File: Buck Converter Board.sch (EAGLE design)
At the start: 6 parts, among them J1 POWERPOLE_POWER25A_HORIZONTAL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, J2 POWERPOLE_POWER25A_HORIZONTAL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

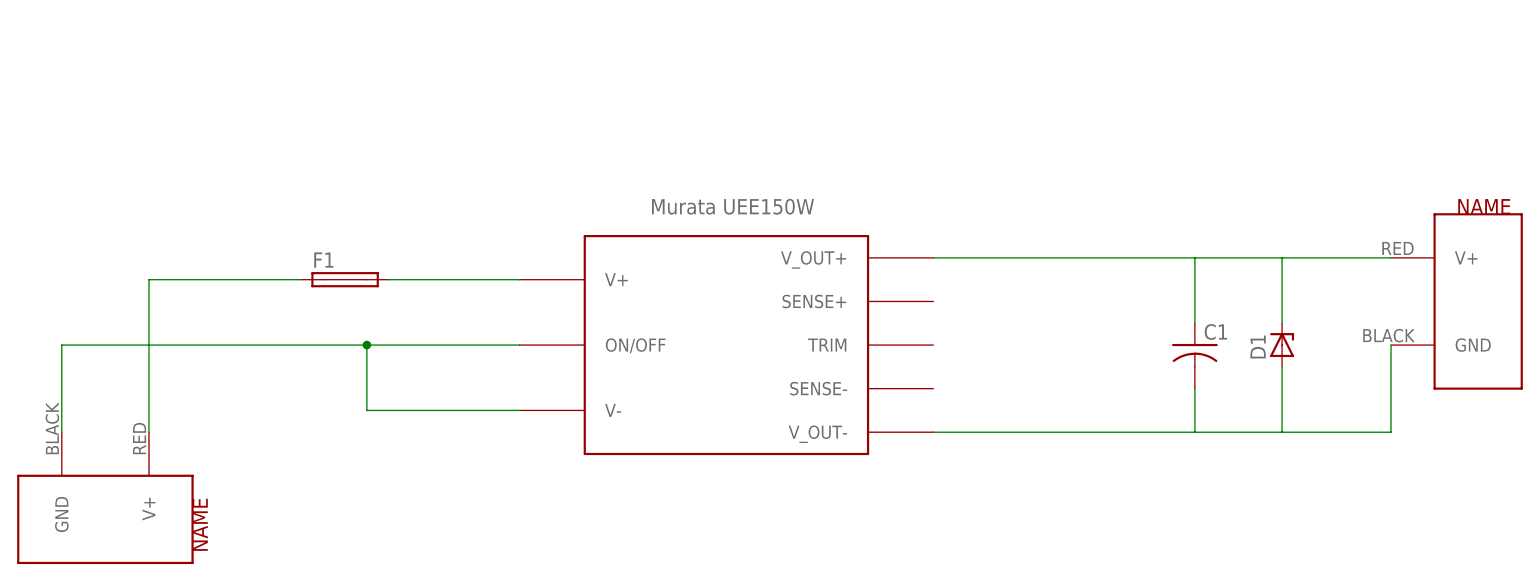
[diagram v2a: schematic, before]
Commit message: routed buck board
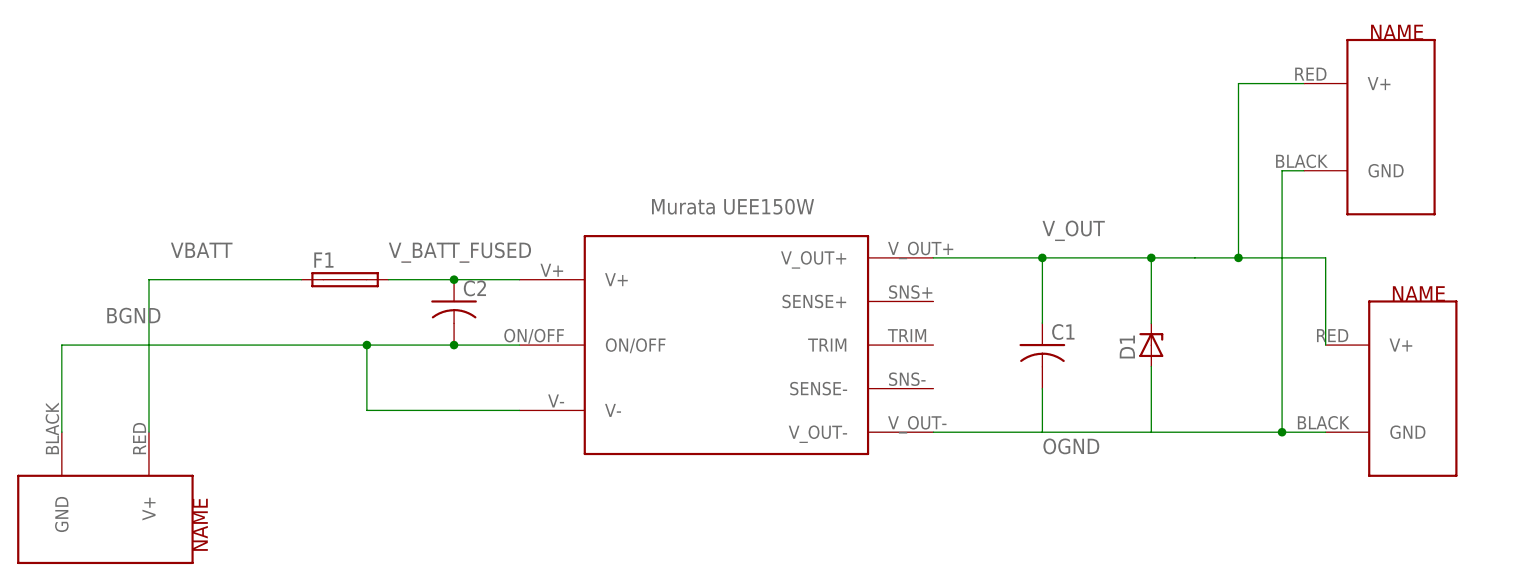
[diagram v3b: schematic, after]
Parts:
- added C2: (no value), rcl:C-USC0805
- added J3: POWERPOLE_POWER25A_HORIZONTAL_G2, powerpoles:POWERPOLE_POWER25A_HORIZONTAL_G2
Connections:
- net N$1 renamed VBATT
- removed net N$11: D1.C
- removed net N$2: F1.2, U$1.V+
- removed net N$3: J1.GND, U$1.ON/OFF, U$1.V-
- removed net N$4: J2.V+, U$1.V_OUT+
- removed net N$5: C1.1
- removed net N$6: C1.2, J2.GND, U$1.V_OUT-
- new net BGND: C2.2, J1.GND, U$1.ON/OFF, U$1.V-
- new net OGND: C1.2, J2.GND, J3.GND, U$1.V_OUT-
- new net V_BATT_FUSED: C2.1, F1.2, U$1.V+
- new net V_OUT: C1.1, D1.C, J2.V+, J3.V+, U$1.V_OUT+
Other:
- moved on the sheet: C1, D1
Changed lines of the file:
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@@
 <part name="J1" library="powerpoles" deviceset="POWERPOLE_POWER" device="25A_HORIZONTAL_G2"/>
 <part name="J2" library="powerpoles" deviceset="POWERPOLE_POWER" device="25A_HORIZONTAL_G2"/>
+<part name="D1" library="diode" library_urn="urn:adsk.eagle:library:210" deviceset="ZENER-DIODE" device="SMB" package3d_urn="urn:adsk.eagle:package:43404/2"/>
+<part name="C2" library="rcl" library_urn="urn:adsk.eagle:library:334" deviceset="C-US" device="C0805" package3d_urn="urn:adsk.eagle:package:23617/2"/>
+<part name="J3" library="powerpoles" deviceset="POWERPOLE_POWER" device="25A_HORIZONTAL_G2"/>
 <part name="U$1" library="REV Aux Circuit" deviceset="UEE150W" device=""/>
-<part name="D1" library="diode" library_urn="urn:adsk.eagle:library:210" deviceset="ZENER-DIODE" device="SMB" package3d_urn="urn:adsk.eagle:package:43404/2"/>
 </parts>
 <sheets>
@@
 <attribute name="NAME" x="29.21" y="64.897" size="1.778" layer="95"/>
 </instance>
-<instance part="C1" gate="G$1" x="132.08" y="55.88"/>
+<instance part="C1" gate="G$1" x="114.3" y="55.88"/>
 <instance part="J1" gate="G$1" x="5.08" y="35.56" rot="R270"/>
-<instance part="J2" gate="G$1" x="165.1" y="60.96"/>
+<instance part="J2" gate="G$1" x="157.48" y="50.8"/>
+<instance part="D1" gate="G$1" x="127" y="55.88" rot="R90"/>
+<instance part="C2" gate="G$1" x="45.72" y="60.96"/>
+<instance part="J3" gate="G$1" x="154.94" y="81.28"/>
 <instance part="U$1" gate="G$1" x="60.96" y="43.18"/>
-<instance part="D1" gate="G$1" x="142.24" y="55.88" rot="R90"/>
 </instances>
 <busses>
 </busses>
 <nets>
-<net name="N$1" class="0">
+<net name="VBATT" class="0">
 <segment>
 <pinref part="J1" gate="G$1" pin="V+"/>
@@
 <wire x1="10.16" y1="45.72" x2="10.16" y2="63.5" width="0.1524" layer="91"/>
 <wire x1="10.16" y1="63.5" x2="27.94" y2="63.5" width="0.1524" layer="91"/>
+<label x="12.7" y="66.04" size="1.778" layer="95"/>
 </segment>
 </net>
-<net name="N$2" class="0">
+<net name="V_BATT_FUSED" class="0">
 <segment>
 <pinref part="F1" gate="G$1" pin="2"/>
-<wire x1="38.1" y1="63.5" x2="53.34" y2="63.5" width="0.1524" layer="91"/>
+<wire x1="38.1" y1="63.5" x2="45.72" y2="63.5" width="0.1524" layer="91"/>
+<pinref part="C2" gate="G$1" pin="1"/>
+<wire x1="45.72" y1="63.5" x2="53.34" y2="63.5" width="0.1524" layer="91"/>
+<junction x="45.72" y="63.5"/>
 <pinref part="U$1" gate="G$1" pin="V+"/>
+<label x="38.1" y="66.04" size="1.778" layer="95"/>
 </segment>
 </net>
-<net name="N$3" class="0">
+<net name="BGND" class="0">
 <segment>
 <pinref part="J1" gate="G$1" pin="GND"/>
@@
 <wire x1="0" y1="55.88" x2="35.56" y2="55.88" width="0.1524" layer="91"/>
 <wire x1="35.56" y1="55.88" x2="35.56" y2="48.26" width="0.1524" layer="91"/>
-<pinref part="U$1" gate="G$1" pin="V-"/>
 <wire x1="35.56" y1="48.26" x2="53.34" y2="48.26" width="0.1524" layer="91"/>
 <junction x="35.56" y="55.88"/>
+<wire x1="35.56" y1="55.88" x2="45.72" y2="55.88" width="0.1524" layer="91"/>
+<pinref part="C2" gate="G$1" pin="2"/>
+<wire x1="45.72" y1="55.88" x2="53.34" y2="55.88" width="0.1524" layer="91"/>
+<junction x="45.72" y="55.88"/>
+<pinref part="U$1" gate="G$1" pin="V-"/>
 <pinref part="U$1" gate="G$1" pin="ON/OFF"/>
-<wire x1="35.56" y1="55.88" x2="53.34" y2="55.88" width="0.1524" layer="91"/>
+<label x="5.08" y="58.42" size="1.778" layer="95"/>
 </segment>
 </net>
-<net name="N$6" class="0">
+<net name="V_OUT" class="0">
 <segment>
-<pinref part="C1" gate="G$1" pin="2"/>
-<wire x1="132.08" y1="50.8" x2="132.08" y2="45.72" width="0.1524" layer="91"/>
-<pinref part="J2" gate="G$1" pin="GND"/>
-<wire x1="154.94" y1="55.88" x2="154.94" y2="45.72" width="0.1524" layer="91"/>
-<wire x1="154.94" y1="45.72" x2="132.08" y2="45.72" width="0.1524" layer="91"/>
-<pinref part="U$1" gate="G$1" pin="V_OUT-"/>
-<wire x1="101.6" y1="45.72" x2="132.08" y2="45.72" width="0.1524" layer="91"/>
-</segment>
-</net>
-<net name="N$4" class="0">
-<segment>
+<wire x1="147.32" y1="55.88" x2="147.32" y2="66.04" width="0.1524" layer="91"/>
+<wire x1="147.32" y1="66.04" x2="137.16" y2="66.04" width="0.1524" layer="91"/>
+<wire x1="137.16" y1="66.04" x2="132.08" y2="66.04" width="0.1524" layer="91"/>
+<wire x1="132.08" y1="66.04" x2="127" y2="66.04" width="0.1524" layer="91"/>
+<pinref part="J2" gate="G$1" pin="V+"/>
+<pinref part="J3" gate="G$1" pin="V+"/>
+<wire x1="127" y1="66.04" x2="114.3" y2="66.04" width="0.1524" layer="91"/>
+<wire x1="114.3" y1="66.04" x2="101.6" y2="66.04" width="0.1524" layer="91"/>
+<wire x1="137.16" y1="66.04" x2="137.16" y2="86.36" width="0.1524" layer="91"/>
+<wire x1="137.16" y1="86.36" x2="144.78" y2="86.36" width="0.1524" layer="91"/>
+<junction x="137.16" y="66.04"/>
 <pinref part="U$1" gate="G$1" pin="V_OUT+"/>
-<wire x1="154.94" y1="66.04" x2="101.6" y2="66.04" width="0.1524" layer="91"/>
-<pinref part="J2" gate="G$1" pin="V+"/>
-</segment>
-</net>
-<net name="N$5" class="0">
-<segment>
+<label x="114.3" y="68.58" size="1.778" layer="95"/>
 <pinref part="C1" gate="G$1" pin="1"/>
-<wire x1="132.08" y1="58.42" x2="132.08" y2="66.04" width="0.1524" layer="91"/>
-</segment>
-</net>
-<net name="N$11" class="0">
-<segment>
+<wire x1="114.3" y1="58.42" x2="114.3" y2="66.04" width="0.1524" layer="91"/>
+<junction x="114.3" y="66.04"/>
 <pinref part="D1" gate="G$1" pin="C"/>
-<wire x1="142.24" y1="58.42" x2="142.24" y2="66.04" width="0.1524" layer="91"/>
+<wire x1="127" y1="58.42" x2="127" y2="66.04" width="0.1524" layer="91"/>
+<junction x="127" y="66.04"/>
 </segment>
 </net>
@@
 <segment>
 <pinref part="D1" gate="G$1" pin="A"/>
-<wire x1="142.24" y1="45.72" x2="142.24" y2="53.34" width="0.1524" layer="91"/>
+<wire x1="127" y1="45.72" x2="127" y2="53.34" width="0.1524" layer="91"/>
 </segment>
 </net>
+<net name="OGND" class="0">
+<segment>
+<pinref part="C1" gate="G$1" pin="2"/>
+<wire x1="114.3" y1="50.8" x2="114.3" y2="45.72" width="0.1524" layer="91"/>
+<pinref part="J2" gate="G$1" pin="GND"/>
+<wire x1="147.32" y1="45.72" x2="142.24" y2="45.72" width="0.1524" layer="91"/>
+<wire x1="142.24" y1="45.72" x2="114.3" y2="45.72" width="0.1524" layer="91"/>
+<wire x1="101.6" y1="45.72" x2="114.3" y2="45.72" width="0.1524" layer="91"/>
+<pinref part="J3" gate="G$1" pin="GND"/>
+<wire x1="142.24" y1="45.72" x2="142.24" y2="76.2" width="0.1524" layer="91"/>
+<wire x1="142.24" y1="76.2" x2="144.78" y2="76.2" width="0.1524" layer="91"/>
+<junction x="142.24" y="45.72"/>
+<pinref part="U$1" gate="G$1" pin="V_OUT-"/>
+<label x="114.3" y="43.18" size="1.778" layer="95"/>
+</segment>
+</net>

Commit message: named nets on buck board
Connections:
- removed net N$12: D1.A
- net OGND: now also D1.A
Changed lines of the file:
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@@
-</segment>
-</net>
-<net name="N$12" class="0">
-<segment>
-<pinref part="D1" gate="G$1" pin="A"/>
-<wire x1="127" y1="45.72" x2="127" y2="53.34" width="0.1524" layer="91"/>
 </segment>
 </net>
@@
 <label x="114.3" y="43.18" size="1.778" layer="95"/>
 </segment>
+<segment>
+<pinref part="D1" gate="G$1" pin="A"/>
+<wire x1="127" y1="45.72" x2="127" y2="53.34" width="0.1524" layer="91"/>
+</segment>
 </net>

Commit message: redid polygon for buck board
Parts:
- renumbered U$1 to UEE150W
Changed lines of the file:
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@@
 <part name="C2" library="rcl" library_urn="urn:adsk.eagle:library:334" deviceset="C-US" device="C0805" package3d_urn="urn:adsk.eagle:package:23617/2"/>
 <part name="J3" library="powerpoles" deviceset="POWERPOLE_POWER" device="25A_HORIZONTAL_G2"/>
-<part name="U$1" library="REV Aux Circuit" deviceset="UEE150W" device=""/>
+<part name="UEE150W" library="REV Aux Circuit" deviceset="UEE150W" device=""/>
 </parts>
 <sheets>
@@
 <instance part="C2" gate="G$1" x="45.72" y="60.96"/>
 <instance part="J3" gate="G$1" x="154.94" y="81.28"/>
-<instance part="U$1" gate="G$1" x="60.96" y="43.18"/>
+<instance part="UEE150W" gate="G$1" x="60.96" y="43.18"/>
 </instances>
 <busses>
@@
 <wire x1="45.72" y1="63.5" x2="53.34" y2="63.5" width="0.1524" layer="91"/>
 <junction x="45.72" y="63.5"/>
-<pinref part="U$1" gate="G$1" pin="V+"/>
+<pinref part="UEE150W" gate="G$1" pin="V+"/>
 <label x="38.1" y="66.04" size="1.778" layer="95"/>
 </segment>
@@
 <wire x1="45.72" y1="55.88" x2="53.34" y2="55.88" width="0.1524" layer="91"/>
 <junction x="45.72" y="55.88"/>
-<pinref part="U$1" gate="G$1" pin="V-"/>
-<pinref part="U$1" gate="G$1" pin="ON/OFF"/>
+<pinref part="UEE150W" gate="G$1" pin="V-"/>
+<pinref part="UEE150W" gate="G$1" pin="ON/OFF"/>
 <label x="5.08" y="58.42" size="1.778" layer="95"/>
 </segment>
@@
 <wire x1="137.16" y1="86.36" x2="144.78" y2="86.36" width="0.1524" layer="91"/>
 <junction x="137.16" y="66.04"/>
-<pinref part="U$1" gate="G$1" pin="V_OUT+"/>
+<pinref part="UEE150W" gate="G$1" pin="V_OUT+"/>
 <label x="114.3" y="68.58" size="1.778" layer="95"/>
 <pinref part="C1" gate="G$1" pin="1"/>
@@
 <wire x1="142.24" y1="76.2" x2="144.78" y2="76.2" width="0.1524" layer="91"/>
 <junction x="142.24" y="45.72"/>
-<pinref part="U$1" gate="G$1" pin="V_OUT-"/>
+<pinref part="UEE150W" gate="G$1" pin="V_OUT-"/>
 <label x="114.3" y="43.18" size="1.778" layer="95"/>
 </segment>

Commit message: Changed diode package, made a trace larger
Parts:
- removed D1: (no value), diode:ZENER-DIODESMB
- added D2: 15KEXX, diode:15KEXX
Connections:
- net OGND: now also D2.A; no longer D1.A
- net V_OUT: now also D2.C; no longer D1.C

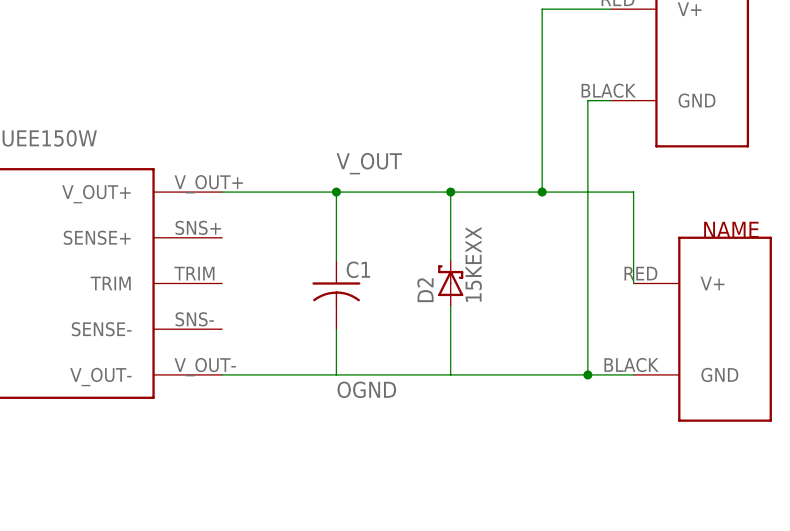
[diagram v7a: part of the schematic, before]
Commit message: connected sense pins on buck board
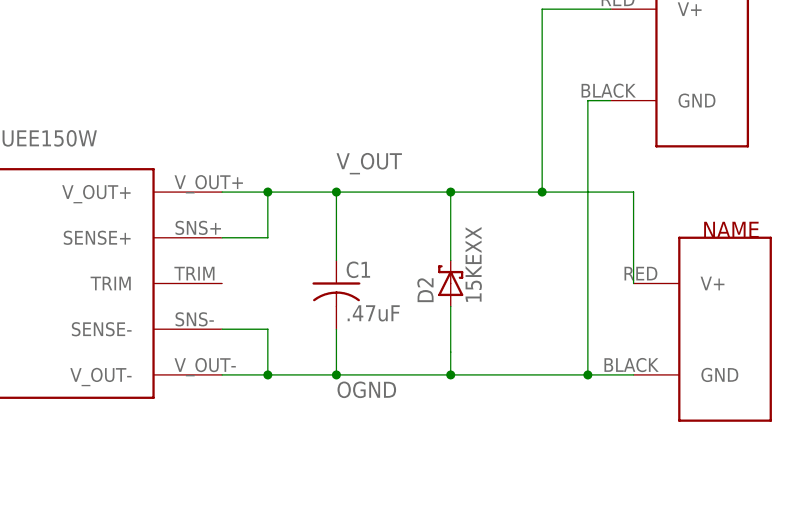
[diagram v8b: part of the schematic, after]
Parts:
- C1: value (none) -> .47uF
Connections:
- net OGND: now also UEE150W.SENSE-
- net V_OUT: now also UEE150W.SENSE+
